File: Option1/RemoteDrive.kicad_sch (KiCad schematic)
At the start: 2 parts, among them Q1001 AON6284

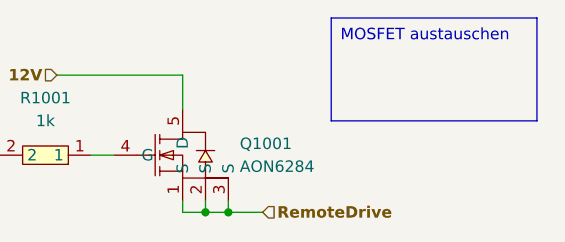
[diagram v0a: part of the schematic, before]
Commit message: SPI Flash hinzugefügt, IN/Outputs vereinheitlicht, USB Flash Möglichkeit hinzugefügt, Display fehtl noch
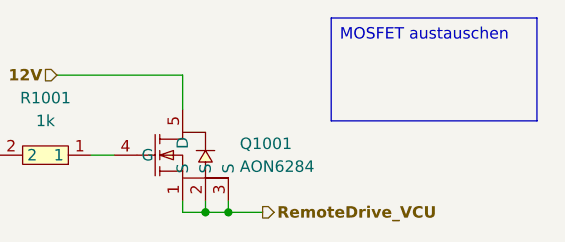
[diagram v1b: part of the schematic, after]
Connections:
- net RemoteDrive renamed RemoteDrive_VCU
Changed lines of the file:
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@@
 (kicad_sch
-	(version 20231120)
+	(version 20250114)
 	(generator "eeschema")
-	(generator_version "8.0")
+	(generator_version "9.0")
 	(paper "A4")
 	(title_block
@@
 		(comment 2 "Bachelorarbiet")
 		(comment 3 "Sebastian Hampl")
+	)
+	(text_box "MOSFET austauschen"
+		(exclude_from_sim no)
+		(at 128.27 55.88 0)
+		(size 22.86 11.43)
+		(margins 0.9525 0.9525 0.9525 0.9525)
+		(stroke
+			(width 0)
+			(type default)
+			(color 255 0 0 1)
+		)
+		(fill
+			(type none)
+		)
+		(effects
+			(font
+				(size 1.27 1.27)
+			)
+			(justify left top)
+		)
 	)
 	(junction
@@
 		)
 	)
-	(text_box "MOSFET austauschen"
-		(exclude_from_sim no)
-		(at 128.27 55.88 0)
-		(size 22.86 11.43)
-		(stroke
-			(width 0)
-			(type default)
-			(color 255 0 0 1)
-		)
-		(fill
-			(type none)
-		)
-		(effects
-			(font
-				(size 1.27 1.27)
-			)
-			(justify left top)
-		)
-	)
-	(hierarchical_label "RemoteDrive"
-		(shape input)
+	(hierarchical_label "RemoteDrive_VCU"
+		(shape output)
 		(at 120.65 77.47 0)
 		(effects

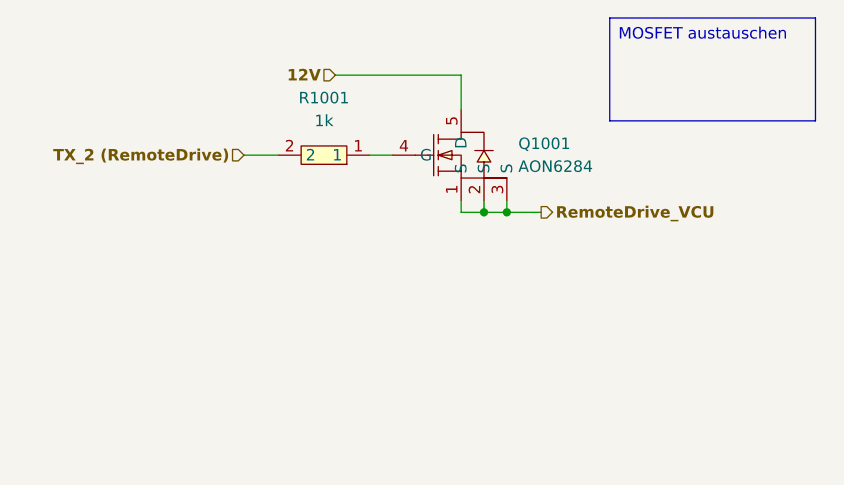
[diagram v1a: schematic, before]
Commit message: USB auf 3V3 umgebaut
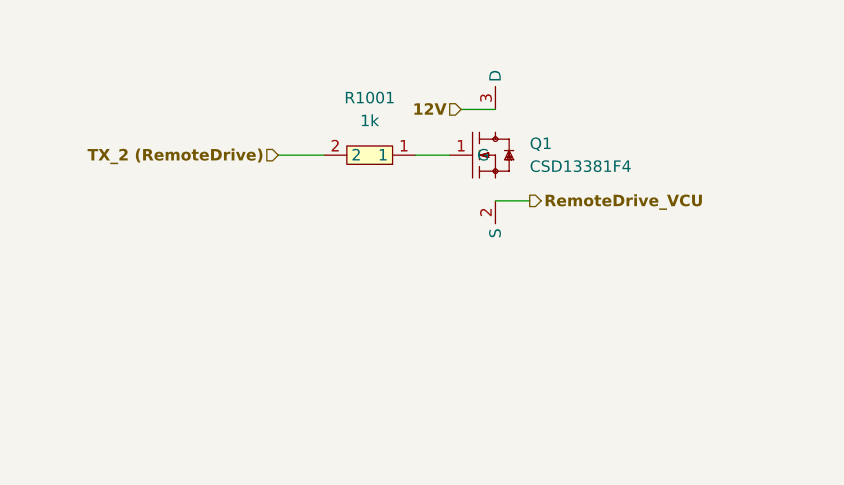
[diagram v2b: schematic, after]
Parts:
- removed Q1001: AON6284, easyeda2kicad:POWERVDFN-8_L6.2-W5.2-P1.27-LS6.0-BL, symbol easyeda2kicad:AON6284
- added Q1: CSD13381F4, easyeda2kicad:PICOSTAR-3_L1.0-W0.6-P0.40-S0.65-BL-1, symbol EasyEda2KiCad:CSD13381F4
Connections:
- net 12V: now also Q1.3 (D)
- net RemoteDrive_VCU: now also Q1.2 (S)
- net at R1001.1: now also Q1.1 (G)
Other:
- moved on the sheet: R1001
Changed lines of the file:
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@@
 		(comment 3 "Sebastian Hampl")
 	)
-	(text_box "MOSFET austauschen"
-		(exclude_from_sim no)
-		(at 128.27 55.88 0)
-		(size 22.86 11.43)
-		(margins 0.9525 0.9525 0.9525 0.9525)
-		(stroke
-			(width 0)
-			(type default)
-			(color 255 0 0 1)
-		)
-		(fill
-			(type none)
-		)
-		(effects
-			(font
-				(size 1.27 1.27)
-			)
-			(justify left top)
-		)
-	)
-	(junction
-		(at 114.3 77.47)
-		(diameter 0)
-		(color 0 0 0 0)
-	)
-	(junction
-		(at 116.84 77.47)
-		(diameter 0)
-		(color 0 0 0 0)
-	)
-	(wire
-		(pts
-			(xy 111.76 77.47) (xy 111.76 76.2)
-		)
-		(stroke
-			(width 0)
-			(type default)
-		)
-	)
-	(wire
-		(pts
-			(xy 111.76 62.23) (xy 111.76 66.04)
-		)
-		(stroke
-			(width 0)
-			(type default)
-		)
-	)
-	(wire
-		(pts
-			(xy 116.84 76.2) (xy 116.84 77.47)
-		)
-		(stroke
-			(width 0)
-			(type default)
-		)
-	)
-	(wire
-		(pts
-			(xy 114.3 76.2) (xy 114.3 77.47)
-		)
-		(stroke
-			(width 0)
-			(type default)
-		)
-	)
-	(wire
-		(pts
-			(xy 97.79 62.23) (xy 111.76 62.23)
-		)
-		(stroke
-			(width 0)
-			(type default)
-		)
-	)
-	(wire
-		(pts
-			(xy 116.84 77.47) (xy 114.3 77.47)
-		)
-		(stroke
-			(width 0)
-			(type default)
-		)
-	)
-	(wire
-		(pts
-			(xy 101.6 71.12) (xy 104.14 71.12)
-		)
-		(stroke
-			(width 0)
-			(type default)
-		)
-	)
-	(wire
-		(pts
-			(xy 114.3 77.47) (xy 111.76 77.47)
-		)
-		(stroke
-			(width 0)
-			(type default)
-		)
-	)
-	(wire
-		(pts
-			(xy 87.63 71.12) (xy 91.44 71.12)
-		)
-		(stroke
-			(width 0)
-			(type default)
-		)
-	)
-	(wire
-		(pts
-			(xy 116.84 77.47) (xy 120.65 77.47)
+	(wire
+		(pts
+			(xy 115.57 66.04) (xy 111.76 66.04)
+		)
+		(stroke
+			(width 0)
+			(type default)
+		)
+	)
+	(wire
+		(pts
+			(xy 106.68 71.12) (xy 110.49 71.12)
+		)
+		(stroke
+			(width 0)
+			(type default)
+		)
+	)
+	(wire
+		(pts
+			(xy 91.44 71.12) (xy 96.52 71.12)
+		)
+		(stroke
+			(width 0)
+			(type default)
+		)
+	)
+	(wire
+		(pts
+			(xy 115.57 76.2) (xy 119.38 76.2)
 		)
 		(stroke
@@
 	(hierarchical_label "RemoteDrive_VCU"
 		(shape output)
-		(at 120.65 77.47 0)
+		(at 119.38 76.2 0)
 		(effects
 			(font
@@
 	(hierarchical_label "12V"
 		(shape input)
-		(at 97.79 62.23 180)
+		(at 111.76 66.04 180)
 		(effects
 			(font
@@
 	(hierarchical_label "TX_2 (RemoteDrive)"
 		(shape input)
-		(at 87.63 71.12 180)
+		(at 91.44 71.12 180)
 		(effects
 			(font
@@
 	(symbol
 		(lib_id "easyeda2kicad:0603WAF1001T5E")
-		(at 96.52 71.12 180)
+		(at 101.6 71.12 180)
 		(unit 1)
 		(exclude_from_sim no)
@@
 		(fields_autoplaced yes)
 		(property "Reference" "R1001"
-			(at 96.52 64.77 0)
+			(at 101.6 64.77 0)
 			(effects
 				(font
@@
 		)
 		(property "Value" "1k"
-			(at 96.52 67.31 0)
+			(at 101.6 67.31 0)
 			(effects
 				(font
@@
 		)
 		(property "Footprint" "easyeda2kicad:R0603"
-			(at 96.52 63.5 0)
+			(at 101.6 63.5 0)
 			(effects
 				(font
@@
 		)
 		(property "Datasheet" "https://lcsc.com/product-detail/Chip-Resistor-Surface-Mount-UniOhm_1KR-1001-1_C21190.html"
-			(at 96.52 60.96 0)
+			(at 101.6 60.96 0)
 			(effects
 				(font
@@
 		)
 		(property "Description" ""
-			(at 96.52 71.12 0)
+			(at 101.6 71.12 0)
 			(effects
 				(font
@@
 		)
 		(property "LCSC Part" "C21190"
-			(at 96.52 58.42 0)
+			(at 101.6 58.42 0)
 			(effects
 				(font
@@
 	)
 	(symbol
-		(lib_id "easyeda2kicad:AON6284")
-		(at 111.76 71.12 0)
+		(lib_id "EasyEda2KiCad:CSD13381F4")
+		(at 113.03 71.12 0)
 		(unit 1)
 		(exclude_from_sim no)
@@
 		(dnp no)
 		(fields_autoplaced yes)
-		(property "Reference" "Q1001"
-			(at 118.11 69.8499 0)
+		(property "Reference" "Q1"
+			(at 119.38 69.8499 0)
 			(effects
 				(font
@@
 			)
 		)
-		(property "Value" "AON6284"
-			(at 118.11 72.3899 0)
+		(property "Value" "CSD13381F4"
+			(at 119.38 72.3899 0)
 			(effects
 				(font
@@
 			)
 		)
-		(property "Footprint" "easyeda2kicad:POWERVDFN-8_L6.2-W5.2-P1.27-LS6.0-BL"
-			(at 111.76 83.82 0)
+		(property "Footprint" "easyeda2kicad:PICOSTAR-3_L1.0-W0.6-P0.40-S0.65-BL-1"
+			(at 113.03 83.82 0)
 			(effects
 				(font
@@
 		)
 		(property "Datasheet" ""
-			(at 111.76 71.12 0)
+			(at 113.03 71.12 0)
 			(effects
 				(font
@@
 		)
 		(property "Description" ""
-			(at 111.76 71.12 0)
-			(effects
-				(font
-					(size 1.27 1.27)
-				)
-				(hide yes)
-			)
-		)
-		(property "LCSC Part" "C3277770"
-			(at 111.76 86.36 0)
-			(effects
-				(font
-					(size 1.27 1.27)
-				)
-				(hide yes)
-			)
-		)
-		(pin "4"
+			(at 113.03 71.12 0)
+			(effects
+				(font
+					(size 1.27 1.27)
+				)
+				(hide yes)
+			)
+		)
+		(property "LCSC Part" "C179868"
+			(at 113.03 86.36 0)
+			(effects
+				(font
+					(size 1.27 1.27)
+				)
+				(hide yes)
+			)
+		)
+		(pin "3"
+		)
+		(pin "1"
 		)
 		(pin "2"
 		)
-		(pin "1"
-		)
-		(pin "3"
-		)
-		(pin "5"
-		)
 		(instances
-			(project "Option1"
+			(project ""
 				(path "/b9e5f262-9648-4b79-bdd1-af888b822329/fdffe3bf-c97d-446e-a60c-6120e9a8e310"
-					(reference "Q1001")
+					(reference "Q1")
 					(unit 1)
 				)

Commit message: Transitor getauscht, Pulldown Widerstände für Definierten LOW Pegel hinzugefügt
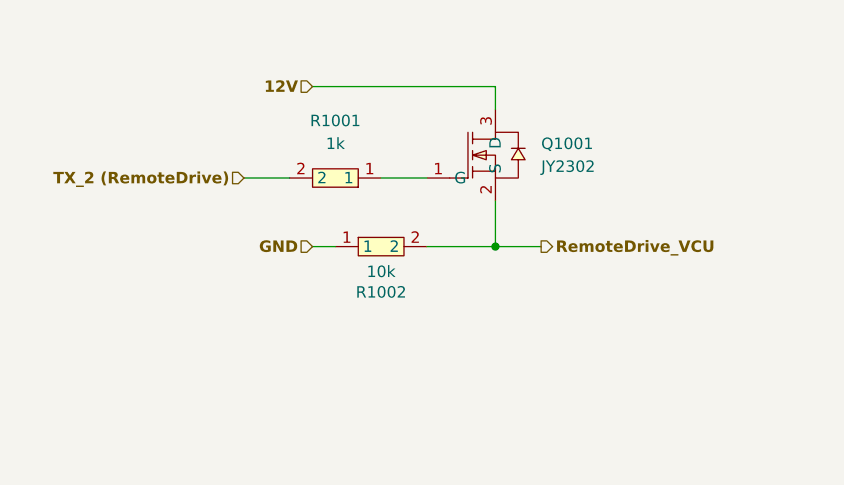
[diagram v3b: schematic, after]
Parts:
- removed Q1: CSD13381F4, easyeda2kicad:PICOSTAR-3_L1.0-W0.6-P0.40-S0.65-BL-1, symbol EasyEda2KiCad:CSD13381F4
- added Q1001: JY2302, easyeda2kicad:SOT-23-3_L2.9-W1.3-P0.95-LS2.4-BR, symbol EasyEda2KiCad:JY2302
- added R1002: 10k, easyeda2kicad:R0603, symbol EasyEda2KiCad:0603WAF1002T5E
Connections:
- net 12V: now also Q1001.3 (D)
- net RemoteDrive_VCU: now also Q1001.2 (S), R1002.2
- net at R1001.1: now also Q1001.1 (G)
- new net GND: R1002.1
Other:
- moved on the sheet: R1001
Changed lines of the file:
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@@
 		(comment 3 "Sebastian Hampl")
 	)
-	(wire
-		(pts
-			(xy 115.57 66.04) (xy 111.76 66.04)
-		)
-		(stroke
-			(width 0)
-			(type default)
-		)
-	)
-	(wire
-		(pts
-			(xy 106.68 71.12) (xy 110.49 71.12)
-		)
-		(stroke
-			(width 0)
-			(type default)
-		)
-	)
-	(wire
-		(pts
-			(xy 91.44 71.12) (xy 96.52 71.12)
-		)
-		(stroke
-			(width 0)
-			(type default)
-		)
-	)
-	(wire
-		(pts
-			(xy 115.57 76.2) (xy 119.38 76.2)
+	(junction
+		(at 115.57 81.28)
+		(diameter 0)
+		(color 0 0 0 0)
+	)
+	(wire
+		(pts
+			(xy 115.57 81.28) (xy 120.65 81.28)
+		)
+		(stroke
+			(width 0)
+			(type default)
+		)
+	)
+	(wire
+		(pts
+			(xy 102.87 73.66) (xy 107.95 73.66)
+		)
+		(stroke
+			(width 0)
+			(type default)
+		)
+	)
+	(wire
+		(pts
+			(xy 115.57 63.5) (xy 95.25 63.5)
+		)
+		(stroke
+			(width 0)
+			(type default)
+		)
+	)
+	(wire
+		(pts
+			(xy 115.57 63.5) (xy 115.57 66.04)
+		)
+		(stroke
+			(width 0)
+			(type default)
+		)
+	)
+	(wire
+		(pts
+			(xy 115.57 76.2) (xy 115.57 81.28)
+		)
+		(stroke
+			(width 0)
+			(type default)
+		)
+	)
+	(wire
+		(pts
+			(xy 95.25 81.28) (xy 97.79 81.28)
+		)
+		(stroke
+			(width 0)
+			(type default)
+		)
+	)
+	(wire
+		(pts
+			(xy 107.95 81.28) (xy 115.57 81.28)
+		)
+		(stroke
+			(width 0)
+			(type default)
+		)
+	)
+	(wire
+		(pts
+			(xy 87.63 73.66) (xy 92.71 73.66)
 		)
 		(stroke
@@
 	(hierarchical_label "RemoteDrive_VCU"
 		(shape output)
-		(at 119.38 76.2 0)
+		(at 120.65 81.28 0)
 		(effects
 			(font
@@
 	(hierarchical_label "12V"
 		(shape input)
-		(at 111.76 66.04 180)
+		(at 95.25 63.5 180)
 		(effects
 			(font
@@
 	(hierarchical_label "TX_2 (RemoteDrive)"
 		(shape input)
-		(at 91.44 71.12 180)
+		(at 87.63 73.66 180)
 		(effects
 			(font
@@
 		)
 	)
+	(hierarchical_label "GND"
+		(shape input)
+		(at 95.25 81.28 180)
+		(effects
+			(font
+				(size 1.27 1.27)
+				(thickness 0.254)
+				(bold yes)
+			)
+			(justify right)
+		)
+	)
+	(symbol
+		(lib_id "EasyEda2KiCad:JY2302")
+		(at 113.03 71.12 0)
+		(unit 1)
+		(exclude_from_sim no)
+		(in_bom yes)
+		(on_board yes)
+		(dnp no)
+		(fields_autoplaced yes)
+		(property "Reference" "Q1001"
+			(at 120.65 69.8499 0)
+			(effects
+				(font
+					(size 1.27 1.27)
+				)
+				(justify left)
+			)
+		)
+		(property "Value" "JY2302"
+			(at 120.65 72.3899 0)
+			(effects
+				(font
+					(size 1.27 1.27)
+				)
+				(justify left)
+			)
+		)
+		(property "Footprint" "easyeda2kicad:SOT-23-3_L2.9-W1.3-P0.95-LS2.4-BR"
+			(at 113.03 83.82 0)
+			(effects
+				(font
+					(size 1.27 1.27)
+				)
+				(hide yes)
+			)
+		)
+		(property "Datasheet" ""
+			(at 113.03 71.12 0)
+			(effects
+				(font
+					(size 1.27 1.27)
+				)
+				(hide yes)
+			)
+		)
+		(property "Description" ""
+			(at 113.03 71.12 0)
+			(effects
+				(font
+					(size 1.27 1.27)
+				)
+				(hide yes)
+			)
+		)
+		(property "LCSC Part" "C3038095"
+			(at 113.03 86.36 0)
+			(effects
+				(font
+					(size 1.27 1.27)
+				)
+				(hide yes)
+			)
+		)
+		(pin "3"
+		)
+		(pin "1"
+		)
+		(pin "2"
+		)
+		(instances
+			(project ""
+				(path "/b9e5f262-9648-4b79-bdd1-af888b822329/fdffe3bf-c97d-446e-a60c-6120e9a8e310"
+					(reference "Q1001")
+					(unit 1)
+				)
+			)
+		)
+	)
 	(symbol
 		(lib_id "easyeda2kicad:0603WAF1001T5E")
-		(at 101.6 71.12 180)
+		(at 97.79 73.66 180)
 		(unit 1)
 		(exclude_from_sim no)
@@
 		(fields_autoplaced yes)
 		(property "Reference" "R1001"
-			(at 101.6 64.77 0)
+			(at 97.79 67.31 0)
 			(effects
 				(font
@@
 		)
 		(property "Value" "1k"
-			(at 101.6 67.31 0)
+			(at 97.79 69.85 0)
 			(effects
 				(font
@@
 		)
 		(property "Footprint" "easyeda2kicad:R0603"
-			(at 101.6 63.5 0)
+			(at 97.79 66.04 0)
 			(effects
 				(font
@@
 		)
 		(property "Datasheet" "https://lcsc.com/product-detail/Chip-Resistor-Surface-Mount-UniOhm_1KR-1001-1_C21190.html"
-			(at 101.6 60.96 0)
+			(at 97.79 63.5 0)
 			(effects
 				(font
@@
 		)
 		(property "Description" ""
-			(at 101.6 71.12 0)
+			(at 97.79 73.66 0)
 			(effects
 				(font
@@
 		)
 		(property "LCSC Part" "C21190"
-			(at 101.6 58.42 0)
+			(at 97.79 60.96 0)
 			(effects
 				(font
@@
 	)
 	(symbol
-		(lib_id "EasyEda2KiCad:CSD13381F4")
-		(at 113.03 71.12 0)
+		(lib_id "EasyEda2KiCad:0603WAF1002T5E")
+		(at 102.87 81.28 0)
 		(unit 1)
 		(exclude_from_sim no)
@@
 		(on_board yes)
 		(dnp no)
-		(fields_autoplaced yes)
-		(property "Reference" "Q1"
-			(at 119.38 69.8499 0)
-			(effects
-				(font
-					(size 1.27 1.27)
-				)
-				(justify left)
-			)
-		)
-		(property "Value" "CSD13381F4"
-			(at 119.38 72.3899 0)
-			(effects
-				(font
-					(size 1.27 1.27)
-				)
-				(justify left)
-			)
-		)
-		(property "Footprint" "easyeda2kicad:PICOSTAR-3_L1.0-W0.6-P0.40-S0.65-BL-1"
-			(at 113.03 83.82 0)
-			(effects
-				(font
-					(size 1.27 1.27)
-				)
-				(hide yes)
-			)
-		)
-		(property "Datasheet" ""
-			(at 113.03 71.12 0)
+		(property "Reference" "R1002"
+			(at 102.87 86.36 0)
+			(effects
+				(font
+					(size 1.27 1.27)
+				)
+			)
+		)
+		(property "Value" "10k"
+			(at 102.87 84.074 0)
+			(effects
+				(font
+					(size 1.27 1.27)
+				)
+			)
+		)
+		(property "Footprint" "easyeda2kicad:R0603"
+			(at 102.87 88.9 0)
+			(effects
+				(font
+					(size 1.27 1.27)
+				)
+				(hide yes)
+			)
+		)
+		(property "Datasheet" "https://lcsc.com/product-detail/Chip-Resistor-Surface-Mount-UniOhm_10KR-1002-1_C25804.html"
+			(at 102.87 91.44 0)
 			(effects
 				(font
@@
 		)
 		(property "Description" ""
-			(at 113.03 71.12 0)
-			(effects
-				(font
-					(size 1.27 1.27)
-				)
-				(hide yes)
-			)
-		)
-		(property "LCSC Part" "C179868"
-			(at 113.03 86.36 0)
-			(effects
-				(font
-					(size 1.27 1.27)
-				)
-				(hide yes)
-			)
-		)
-		(pin "3"
+			(at 102.87 81.28 0)
+			(effects
+				(font
+					(size 1.27 1.27)
+				)
+				(hide yes)
+			)
+		)
+		(property "LCSC Part" "C25804"
+			(at 102.87 93.98 0)
+			(effects
+				(font
+					(size 1.27 1.27)
+				)
+				(hide yes)
+			)
 		)
 		(pin "1"
@@
 		)
 		(instances
-			(project ""
+			(project "Option1"
 				(path "/b9e5f262-9648-4b79-bdd1-af888b822329/fdffe3bf-c97d-446e-a60c-6120e9a8e310"
-					(reference "Q1")
+					(reference "R1002")
 					(unit 1)
 				)

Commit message: LEDs an Transistoren hinzugefügt, Layout angepasst, LEDs eingefügt, LEDs zeigen an, ob Transsitor durchgeschalten ist
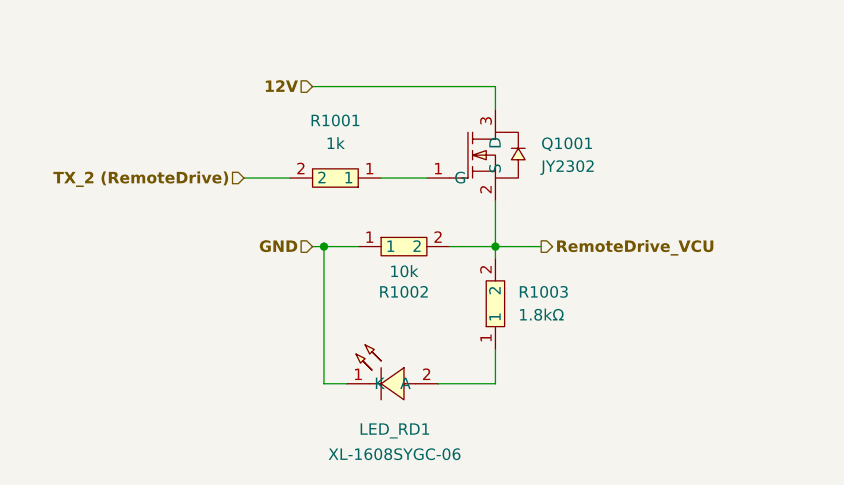
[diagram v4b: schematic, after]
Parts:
- added LED_RD1: XL-1608SYGC-06, easyeda2kicad:LED0603-RD_GREEN, symbol EasyEda2KiCad:XL-1608SYGC-06
- added R1003: 1.8kΩ, easyeda2kicad:R0603, symbol EasyEda2KiCad:0603WAF1801T5E
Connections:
- net GND: now also LED_RD1.1 (K)
- net RemoteDrive_VCU: now also R1003.2
- new net: LED_RD1.2 (A), R1003.1
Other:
- moved on the sheet: R1002
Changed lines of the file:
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@@
 		(color 0 0 0 0)
 	)
+	(junction
+		(at 96.52 81.28)
+		(diameter 0)
+		(color 0 0 0 0)
+	)
 	(wire
 		(pts
@@
 	(wire
 		(pts
+			(xy 96.52 96.52) (xy 96.52 81.28)
+		)
+		(stroke
+			(width 0)
+			(type default)
+		)
+	)
+	(wire
+		(pts
 			(xy 102.87 73.66) (xy 107.95 73.66)
 		)
@@
 	(wire
 		(pts
+			(xy 115.57 82.55) (xy 115.57 81.28)
+		)
+		(stroke
+			(width 0)
+			(type default)
+		)
+	)
+	(wire
+		(pts
 			(xy 115.57 76.2) (xy 115.57 81.28)
 		)
@@
 	(wire
 		(pts
-			(xy 95.25 81.28) (xy 97.79 81.28)
-		)
-		(stroke
-			(width 0)
-			(type default)
-		)
-	)
-	(wire
-		(pts
-			(xy 107.95 81.28) (xy 115.57 81.28)
+			(xy 96.52 81.28) (xy 100.33 81.28)
+		)
+		(stroke
+			(width 0)
+			(type default)
+		)
+	)
+	(wire
+		(pts
+			(xy 115.57 92.71) (xy 115.57 96.52)
+		)
+		(stroke
+			(width 0)
+			(type default)
+		)
+	)
+	(wire
+		(pts
+			(xy 95.25 81.28) (xy 96.52 81.28)
+		)
+		(stroke
+			(width 0)
+			(type default)
+		)
+	)
+	(wire
+		(pts
+			(xy 99.06 96.52) (xy 96.52 96.52)
+		)
+		(stroke
+			(width 0)
+			(type default)
+		)
+	)
+	(wire
+		(pts
+			(xy 110.49 81.28) (xy 115.57 81.28)
 		)
 		(stroke
@@
 		(pts
 			(xy 87.63 73.66) (xy 92.71 73.66)
+		)
+		(stroke
+			(width 0)
+			(type default)
+		)
+	)
+	(wire
+		(pts
+			(xy 109.22 96.52) (xy 115.57 96.52)
 		)
 		(stroke
@@
 			)
 			(justify right)
+		)
+	)
+	(symbol
+		(lib_id "EasyEda2KiCad:XL-1608SYGC-06")
+		(at 104.14 96.52 0)
+		(unit 1)
+		(exclude_from_sim no)
+		(in_bom yes)
+		(on_board yes)
+		(dnp no)
+		(property "Reference" "LED_RD1"
+			(at 104.394 101.6 0)
+			(effects
+				(font
+					(size 1.27 1.27)
+				)
+			)
+		)
+		(property "Value" "XL-1608SYGC-06"
+			(at 104.394 104.394 0)
+			(effects
+				(font
+					(size 1.27 1.27)
+				)
+			)
+		)
+		(property "Footprint" "easyeda2kicad:LED0603-RD_GREEN"
+			(at 104.14 104.14 0)
+			(effects
+				(font
+					(size 1.27 1.27)
+				)
+				(hide yes)
+			)
+		)
+		(property "Datasheet" ""
+			(at 104.14 96.52 0)
+			(effects
+				(font
+					(size 1.27 1.27)
+				)
+				(hide yes)
+			)
+		)
+		(property "Description" ""
+			(at 104.14 96.52 0)
+			(effects
+				(font
+					(size 1.27 1.27)
+				)
+				(hide yes)
+			)
+		)
+		(property "LCSC Part" "C965805"
+			(at 104.14 106.68 0)
+			(effects
+				(font
+					(size 1.27 1.27)
+				)
+				(hide yes)
+			)
+		)
+		(pin "2"
+		)
+		(pin "1"
+		)
+		(instances
+			(project "Option1"
+				(path "/b9e5f262-9648-4b79-bdd1-af888b822329/fdffe3bf-c97d-446e-a60c-6120e9a8e310"
+					(reference "LED_RD1")
+					(unit 1)
+				)
+			)
 		)
 	)
@@
 	(symbol
 		(lib_id "EasyEda2KiCad:0603WAF1002T5E")
-		(at 102.87 81.28 0)
+		(at 105.41 81.28 0)
 		(unit 1)
 		(exclude_from_sim no)
@@
 		(dnp no)
 		(property "Reference" "R1002"
-			(at 102.87 86.36 0)
+			(at 105.41 86.36 0)
 			(effects
 				(font
@@
 		)
 		(property "Value" "10k"
-			(at 102.87 84.074 0)
+			(at 105.41 84.074 0)
 			(effects
 				(font
@@
 		)
 		(property "Footprint" "easyeda2kicad:R0603"
-			(at 102.87 88.9 0)
+			(at 105.41 88.9 0)
 			(effects
 				(font
@@
 		)
 		(property "Datasheet" "https://lcsc.com/product-detail/Chip-Resistor-Surface-Mount-UniOhm_10KR-1002-1_C25804.html"
-			(at 102.87 91.44 0)
+			(at 105.41 91.44 0)
 			(effects
 				(font
@@
 		)
 		(property "Description" ""
-			(at 102.87 81.28 0)
+			(at 105.41 81.28 0)
 			(effects
 				(font
@@
 		)
 		(property "LCSC Part" "C25804"
-			(at 102.87 93.98 0)
+			(at 105.41 93.98 0)
 			(effects
 				(font
@@
 					(unit 1)
 				)
+			)
+		)
+	)
+	(symbol
+		(lib_id "EasyEda2KiCad:0603WAF1801T5E")
+		(at 115.57 87.63 90)
+		(unit 1)
+		(exclude_from_sim no)
+		(in_bom yes)
+		(on_board yes)
+		(dnp no)
+		(fields_autoplaced yes)
+		(property "Reference" "R1003"
+			(at 118.11 86.3599 90)
+			(effects
+				(font
+					(size 1.27 1.27)
+				)
+				(justify right)
+			)
+		)
+		(property "Value" "1.8kΩ"
+			(at 118.11 88.8999 90)
+			(effects
+				(font
+					(size 1.27 1.27)
+				)
+				(justify right)
+			)
+		)
+		(property "Footprint" "easyeda2kicad:R0603"
+			(at 123.19 87.63 0)
+			(effects
+				(font
+					(size 1.27 1.27)
+				)
+				(hide yes)
+			)
+		)
+		(property "Datasheet" "https://lcsc.com/product-detail/Chip-Resistor-Surface-Mount-UniOhm_1-8KR-1801-1_C4177.html"
+			(at 125.73 87.63 0)
+			(effects
+				(font
+					(size 1.27 1.27)
+				)
+				(hide yes)
+			)
+		)
+		(property "Description" ""
+			(at 115.57 87.63 0)
+			(effects
+				(font
+					(size 1.27 1.27)
+				)
+				(hide yes)
+			)
+		)
+		(property "LCSC Part" "C4177"
+			(at 128.27 87.63 0)
+			(effects
+				(font
+					(size 1.27 1.27)
+				)
+				(hide yes)
+			)
+		)
+		(pin "1"
+		)
+		(pin "2"
+		)
+		(instances
+			(project "Option1"
+				(path "/b9e5f262-9648-4b79-bdd1-af888b822329/fdffe3bf-c97d-446e-a60c-6120e9a8e310"
+					(reference "R1003")
+					(unit 1)
+				)
